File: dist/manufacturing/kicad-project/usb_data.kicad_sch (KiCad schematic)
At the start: 8 parts, among them J10 USB4105-GF-A

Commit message: Review sourcing replacements and document programming and hardware acceptance
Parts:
- removed J10: USB4105-GF-A, USB4105-GF-A, symbol Device:J_USB4105-GF-A
- added J10: USB4105-GF-A-060, USB4105-GF-A-060, symbol Device:J_USB4105-GF-A-060
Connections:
- net DATA_CC1: now also J10.15 (CC1)
- net DATA_CC2: now also J10.9 (CC2)
- net GND: now also J10.1 (EH1), J10.19 (GND1), J10.2 (GND1), J10.20 (GND1), J10.3 (GND1), J10.4 (GND1), J10.5 (GND1), J10.6 (GND1)
- net USB_DATA_VBUS: now also J10.17 (VBUS), J10.18 (VBUS), J10.7 (VBUS), J10.8 (VBUS)
- net USB_DM_CONN: now also J10.12 (DM), J10.14 (DM)
- net USB_DP_CONN: now also J10.11 (DP), J10.13 (DP)
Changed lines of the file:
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@@
     (instances
       (project ""
-        (path "/d02b7698-2cde-4935-ad58-c5f3512e3d51/39e2d365-4459-495a-a3ab-95027c182e4f"
+        (path "/ae2c2659-56b5-4aaf-8217-aebf28b367e8/0738e3ca-62a4-4769-ad44-559694d8095b"
           (reference "R107")
           (unit 1)
@@
     (instances
       (project ""
-        (path "/d02b7698-2cde-4935-ad58-c5f3512e3d51/39e2d365-4459-495a-a3ab-95027c182e4f"
+        (path "/ae2c2659-56b5-4aaf-8217-aebf28b367e8/0738e3ca-62a4-4769-ad44-559694d8095b"
           (reference "R108")
           (unit 1)
@@
     (instances
       (project ""
-        (path "/d02b7698-2cde-4935-ad58-c5f3512e3d51/39e2d365-4459-495a-a3ab-95027c182e4f"
+        (path "/ae2c2659-56b5-4aaf-8217-aebf28b367e8/0738e3ca-62a4-4769-ad44-559694d8095b"
           (reference "C72")
           (unit 1)
@@
   )
   (symbol
-    (lib_id "Device:J_USB4105-GF-A")
+    (lib_id "Device:J_USB4105-GF-A-060")
     (at 53.34 48.26 0)
     (unit 1)
@@
       )
     )
-    (property "Value" "USB4105-GF-A"
+    (property "Value" "USB4105-GF-A-060"
       (id 1)
       (at 42.375 20.749999999999986 0)
@@
       )
     )
-    (property "Footprint" "USB4105-GF-A"
+    (property "Footprint" "USB4105-GF-A-060"
       (id 2)
       (at 51.097 48.5 90)
@@
     (instances
       (project ""
-        (path "/d02b7698-2cde-4935-ad58-c5f3512e3d51/39e2d365-4459-495a-a3ab-95027c182e4f"
+        (path "/ae2c2659-56b5-4aaf-8217-aebf28b367e8/0738e3ca-62a4-4769-ad44-559694d8095b"
           (reference "J10")
           (unit 1)
@@
     (instances
       (project ""
-        (path "/d02b7698-2cde-4935-ad58-c5f3512e3d51/39e2d365-4459-495a-a3ab-95027c182e4f"
+        (path "/ae2c2659-56b5-4aaf-8217-aebf28b367e8/0738e3ca-62a4-4769-ad44-559694d8095b"
           (reference "R105")
           (unit 1)
@@
     (instances
       (project ""
-        (path "/d02b7698-2cde-4935-ad58-c5f3512e3d51/39e2d365-4459-495a-a3ab-95027c182e4f"
+        (path "/ae2c2659-56b5-4aaf-8217-aebf28b367e8/0738e3ca-62a4-4769-ad44-559694d8095b"
           (reference "R106")
           (unit 1)
@@
     (instances
       (project ""
-        (path "/d02b7698-2cde-4935-ad58-c5f3512e3d51/39e2d365-4459-495a-a3ab-95027c182e4f"
+        (path "/ae2c2659-56b5-4aaf-8217-aebf28b367e8/0738e3ca-62a4-4769-ad44-559694d8095b"
           (reference "D15")
           (unit 1)
@@
     (instances
       (project ""
-        (path "/d02b7698-2cde-4935-ad58-c5f3512e3d51/39e2d365-4459-495a-a3ab-95027c182e4f"
+        (path "/ae2c2659-56b5-4aaf-8217-aebf28b367e8/0738e3ca-62a4-4769-ad44-559694d8095b"
           (reference "C73")
           (unit 1)

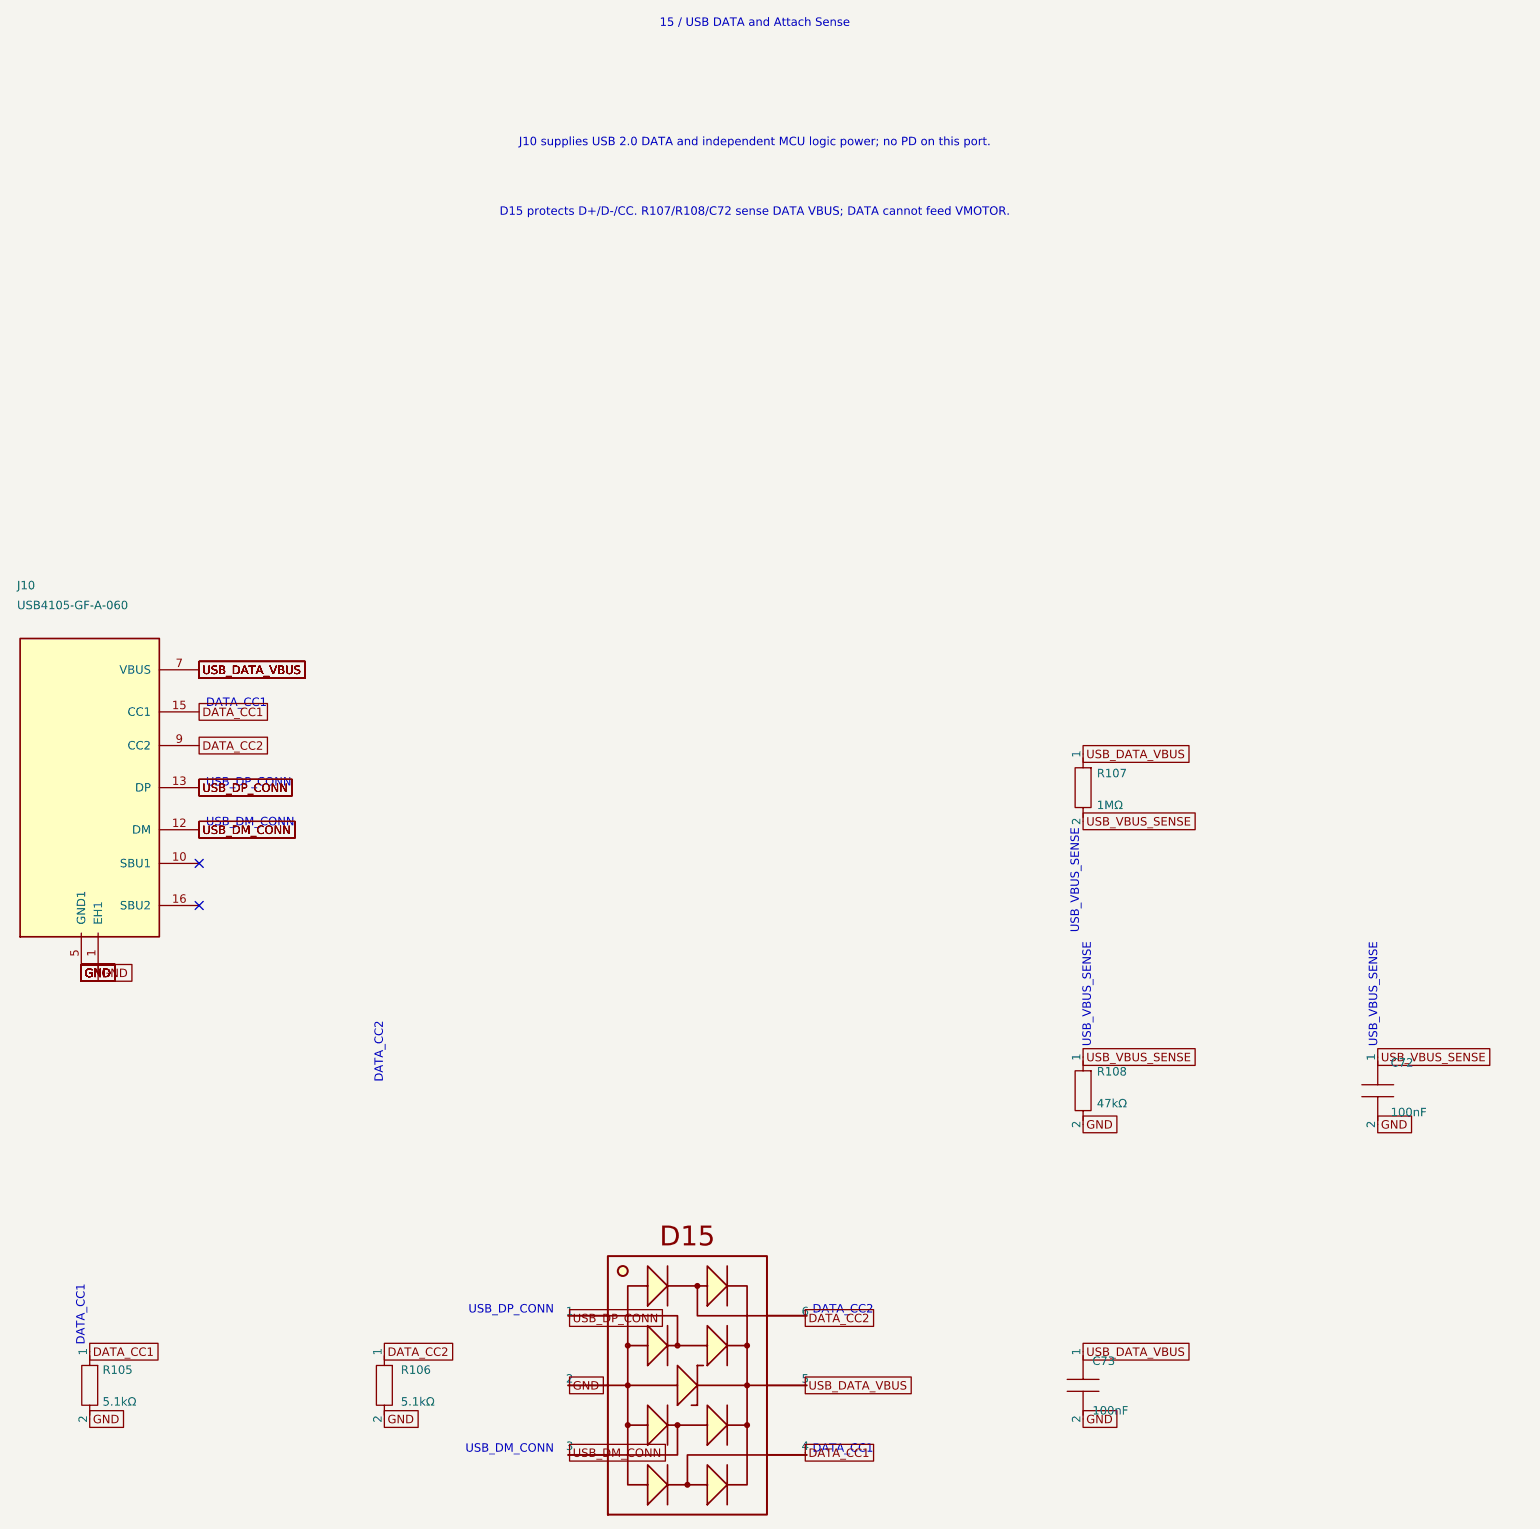
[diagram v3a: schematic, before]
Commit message: Replace unavailable MCU and expander with stocked JLC parts
Use STM32G0B1CEU6 with a grounded UFQFPN48 exposed pad and a 512 KiB
firmware/readback target. Use PCA9538PWR with a PD-powered reset buffer,
bypass capacitor and pulldown to address independent-rail reset injection.

Regenerate local routing, native/manufacturing artifacts, assembly data,
stock evidence and the routed viewer. Preserve unrelated copper and holes
with the existing protected projection. Retain motion locks and physical
qualification holds. Preserve quoted DSN net names and native EP paste sizing.
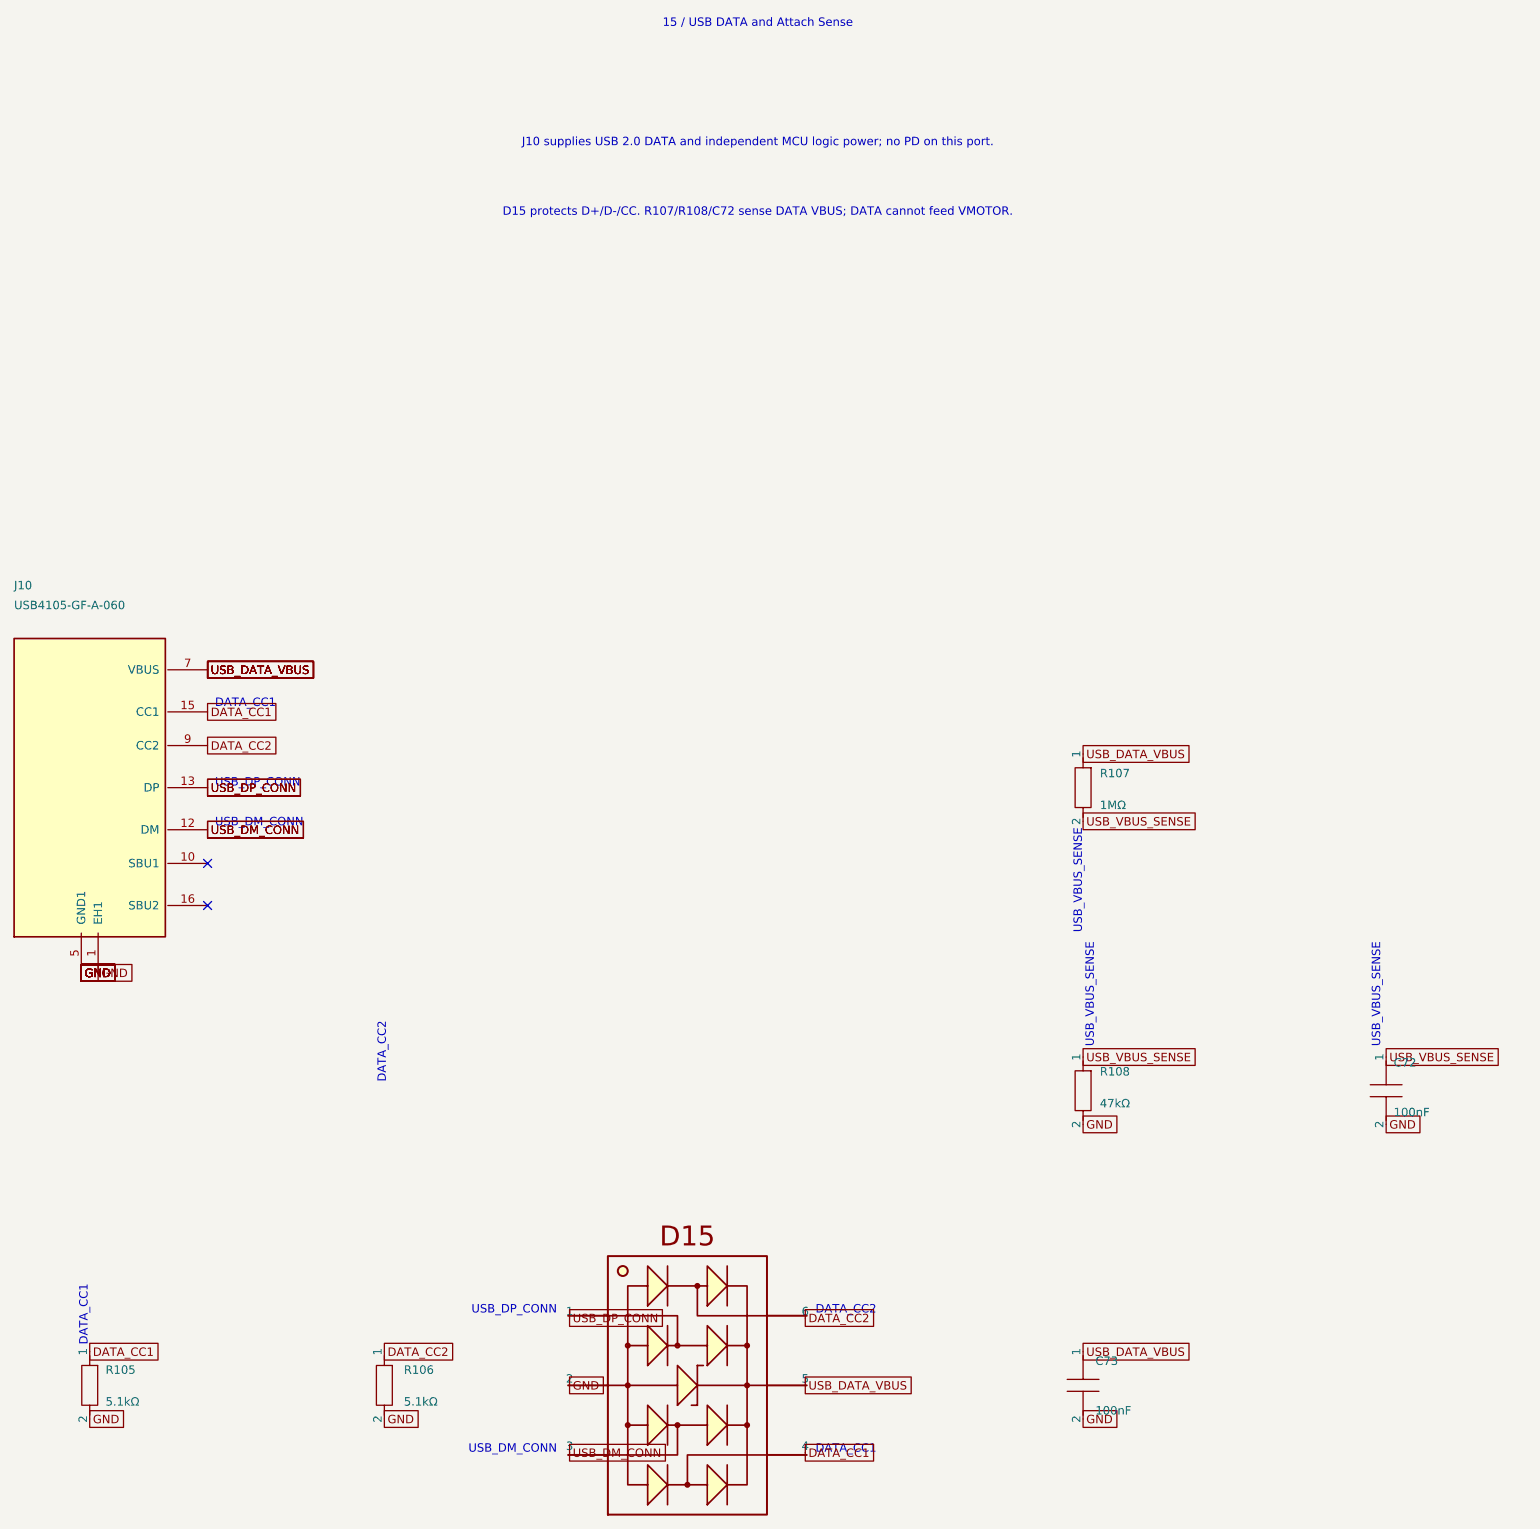
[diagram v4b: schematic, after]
